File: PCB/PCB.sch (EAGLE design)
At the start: 43 parts, among them Q1 11.0592MHz

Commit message: Added adithya's files after verification
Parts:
- added PLED: (no value), led:LED5MM
- C4: value 10nF -> 0.1uF
- R1, R10, R11, R6, R7, R8: value (none) -> 10k
- R12, R17, R5: value (none) -> 1k
- R13, R14, R15, R2, R3, R4: value (none) -> 4.7k
- R9: value (none) -> 2.7k
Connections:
- removed net 555_O/P: 555_TIMER.3, R12.2
- new net N$15: PLED.A, R17.1
- net +10V: now also R14.1; no longer R15.1, R8.1
- net +5V: now also R17.2; no longer CD4029_1.10, CD4029_1.9, CD4029_2.10, CD4029_2.9
- net -10V: now also R8.1
- net A2: now also CD4029_2.14; no longer CD4029_2.11
- net A3: now also CD4029_2.11; no longer CD4029_2.14
- net CLK: now also 555_TIMER.3; no longer R12.1, R13.2
- net GND: now also CD4029_1.10, CD4029_1.9, CD4029_2.10, CD4029_2.9, PLED.C, R12.2, R16.1; no longer R14.1, R17.1
- net IOUT2: now also R15.2; no longer R16.2
- net N$11: now also R13.2; no longer R14.2
- net N$12: now also R14.2; no longer R15.2
- net N$33: now also R16.2; no longer R17.2
- net OUTPUT: now also R12.1, R15.1; no longer R16.1
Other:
- moved on the sheet: R12, R13, R14, R15, R16, R17, TP2

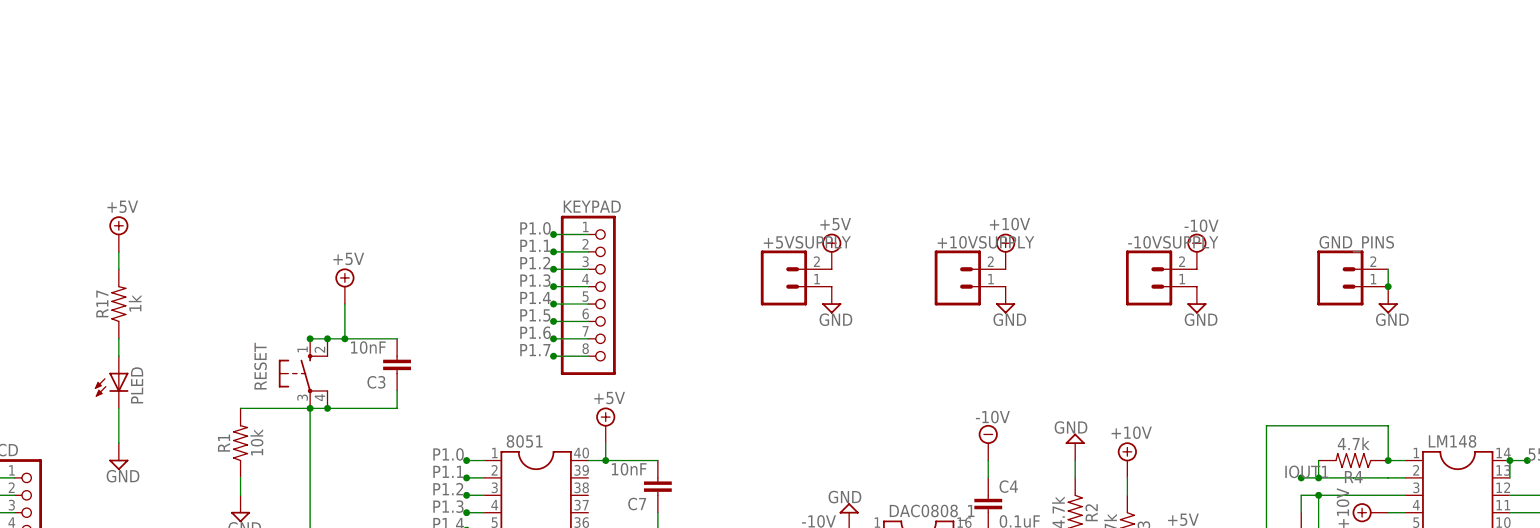
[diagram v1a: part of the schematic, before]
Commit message: Silkscreen, mounting holes, power/ip screw terminals
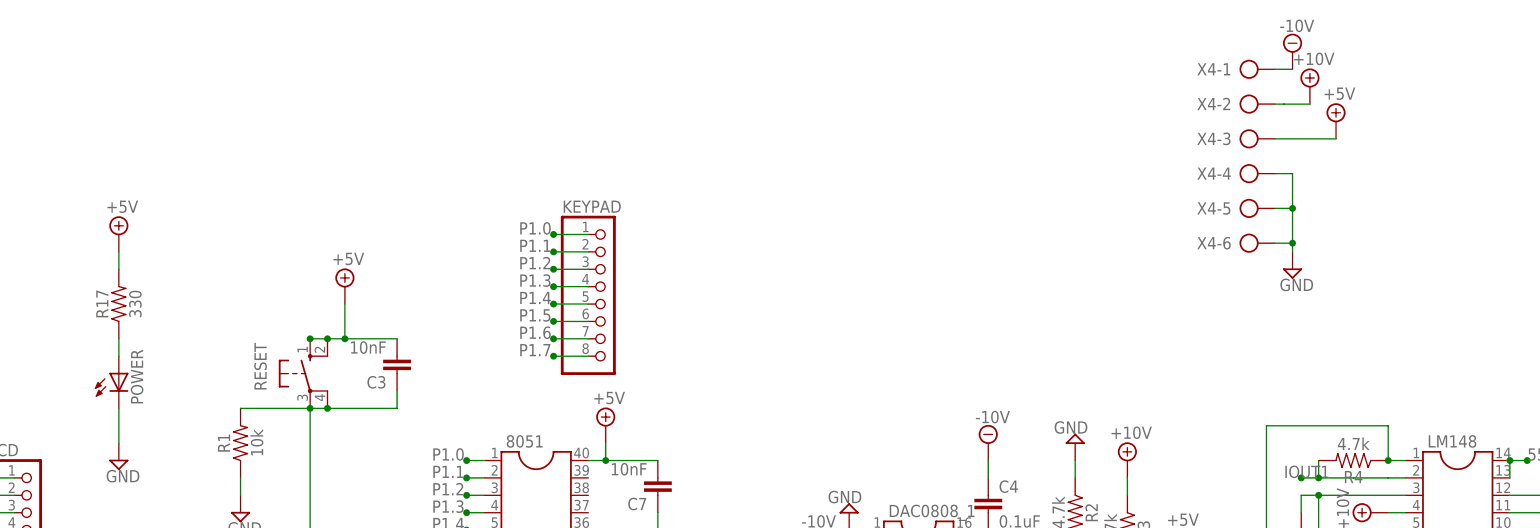
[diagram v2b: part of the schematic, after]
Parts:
- removed +10VSUPPLY, +5VSUPPLY, -10VSUPPLY, GND_PINS: (no value), SparkFun-Connectors:CONN_02
- added X4: (no value), con-ptr500:AK500/6-H
- R17: value 1k -> 330
- renumbered PLED to POWER
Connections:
- net +10V: now also X4-2.KL; no longer +10VSUPPLY.2
- net +5V: now also X4-3.KL; no longer +5VSUPPLY.2
- net -10V: now also X4-1.KL; no longer -10VSUPPLY.2
- net GND: now also X4-4.KL, X4-5.KL, X4-6.KL; no longer +10VSUPPLY.1, +5VSUPPLY.1, -10VSUPPLY.1, GND_PINS.1, GND_PINS.2

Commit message: Final-for manufacturing
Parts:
- added C8: 10nF, rcl:C-EU025-025X050
- added JP1, JP2, SJ1, SJ2, SJ3, SJ4, SJ5, SJ6, SJ7, SJ8: (no value), jumper:SJ
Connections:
- new net CD1-CLK: CD4029_1.15, SJ8.1
- new net CD2-CLK: CD4029_2.15, SJ5.1
- new net N$16: DAC0808_1.14, SJ2.1
- new net OP-555-CTRL: LM148.13, LM148.14, SJ6.1
- new net OPAMP-O/P: IC741.6, JP1.2, R12.1, R15.1, SJ3.1
- net +5V: now also JP2.2
- net 555_CONTROL: now also SJ6.2, SJ7.2; no longer LM148.13, LM148.14
- net CLK: now also SJ5.2, SJ8.2; no longer CD4029_1.15, CD4029_2.15
- net GND: now also C8.1, JP1.1, SJ1.1, SJ4.1, SJ7.1
- net N$2: now also SJ2.2; no longer DAC0808_1.14
- net N$4: now also SJ4.2
- net N$5: now also SJ1.2
- net OUTPUT: now also C8.2, SJ3.2; no longer IC741.6, R12.1, R15.1
- net RESET: now also JP2.1
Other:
- moved on the sheet: TP1

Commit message: Commit since not sure if any changes are made
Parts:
- 555_TIMER, C1, C2, C3, C4, C5, C6, C7, CD4029_1, CD4029_2, D1, DAC0808_1, DAC0808_2, IC741, JP1, JP2, KEYPAD, LCD, LM148, POWER, R1, R10, R11, R12, R13, R14, R15, R16, R17, R2, R3, R4, R5, R6, R7, R8, R9, SJ1, SJ2, SJ3, SJ4, SJ5, SJ6, SJ7, SJ8, TP1, TP2, X4: OC_FARNELL (none) -> unknown
- 8051: MF (none) -> OLIMEX; MPN (none) -> PIC-USB-4550; OC_FARNELL (none) -> 1701541
- C8: value 10nF -> .1u; OC_FARNELL (none) -> unknown
- Q1: MF (none) -> MULTICOMP; MPN (none) -> HC49SM-3.6864-30-50-60-16-ATF
- RESET: MF (none) -> OMRON

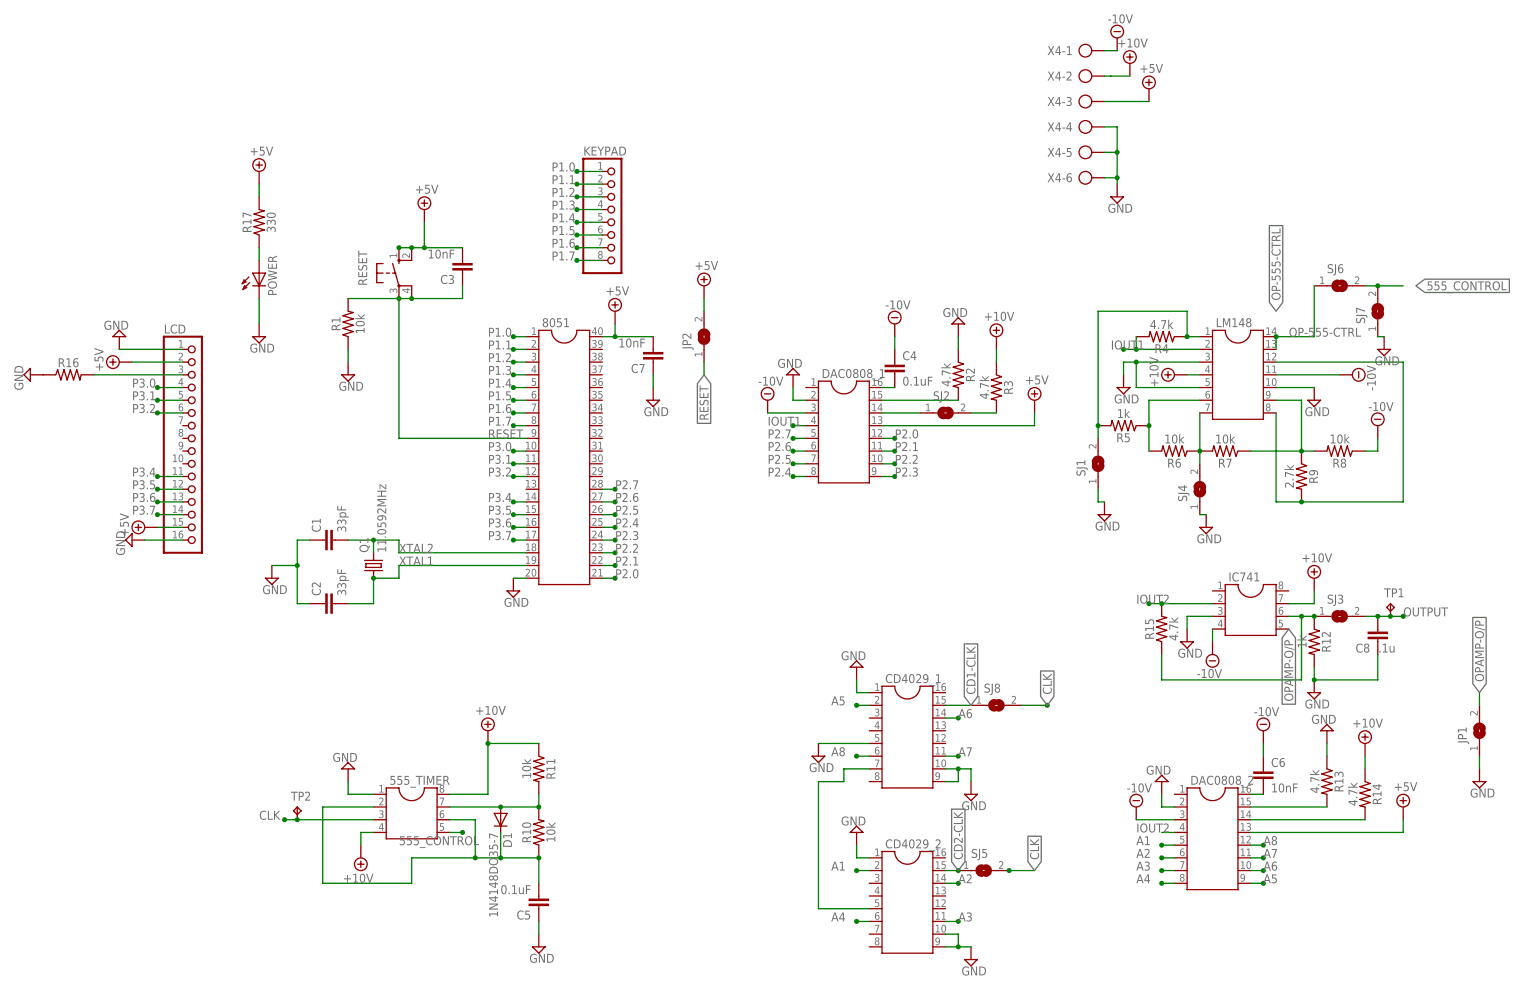
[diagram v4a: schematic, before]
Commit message: During assembly - changed some values
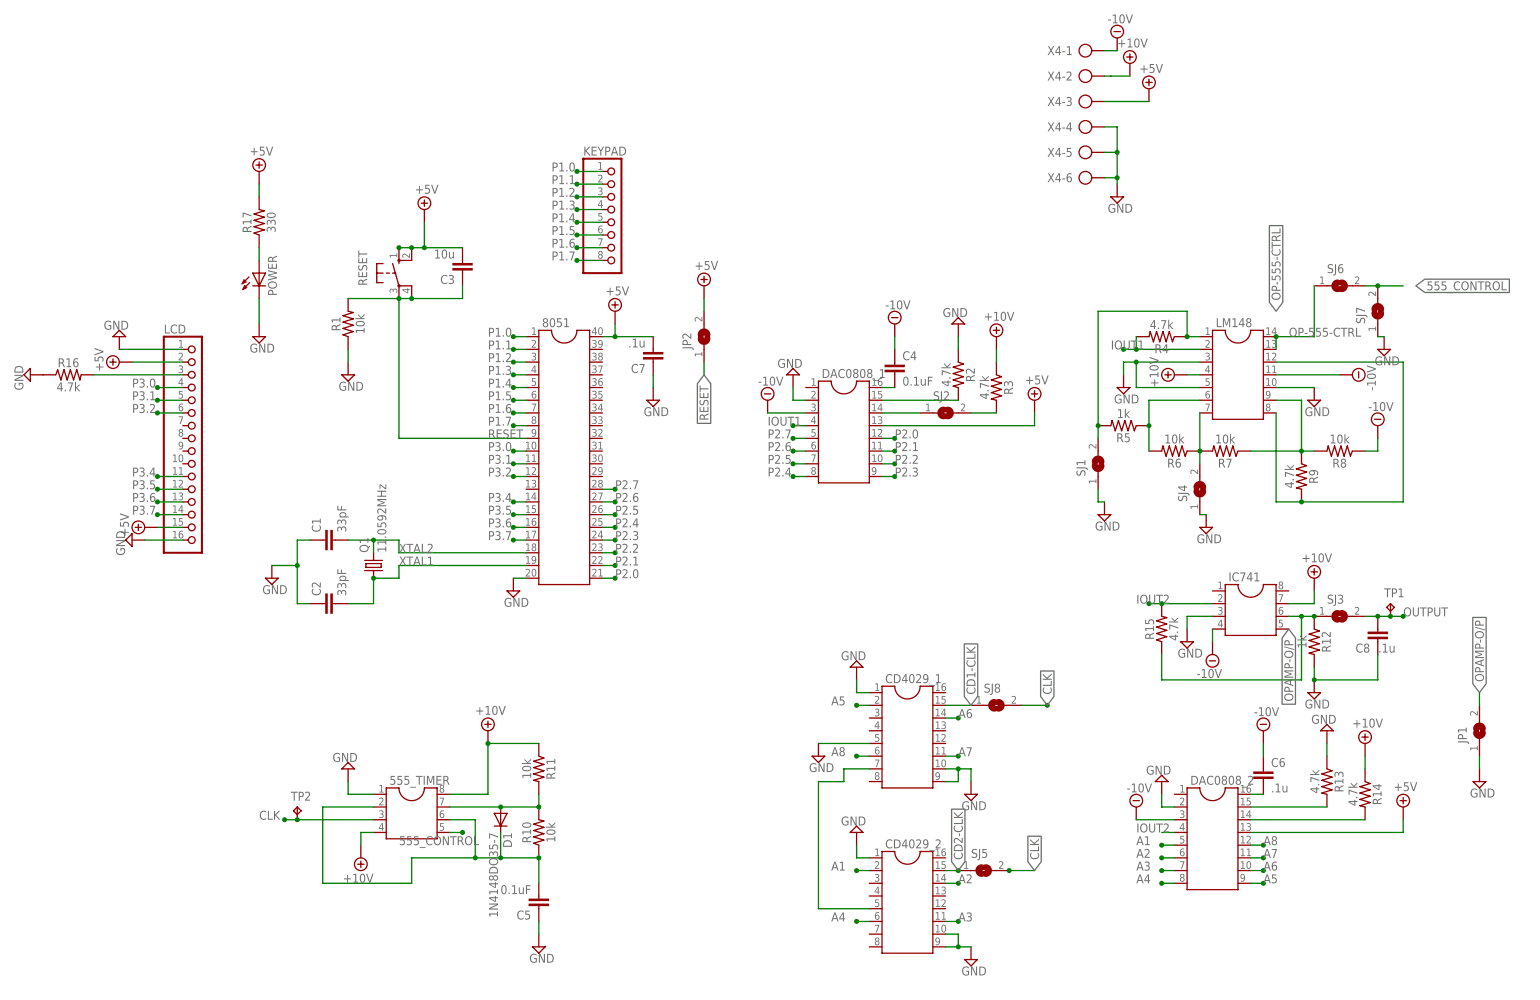
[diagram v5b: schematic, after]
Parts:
- C3: value 10nF -> 10u
- C6, C7: value 10nF -> .1u
- R16: value (none) -> 4.7k
- R9: value 2.7k -> 4.7k
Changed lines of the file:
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@@
 <attribute name="OC_FARNELL" value="unknown"/>
 </part>
-<part name="C3" library="rcl" library_urn="urn:adsk.eagle:library:334" deviceset="C-EU" device="025-025X050" package3d_urn="urn:adsk.eagle:package:23629/2" value="10nF">
+<part name="C3" library="rcl" library_urn="urn:adsk.eagle:library:334" deviceset="C-EU" device="025-025X050" package3d_urn="urn:adsk.eagle:package:23629/2" value="10u">
 <spice>
 <pinmapping spiceprefix="C">
@@
 <attribute name="OC_FARNELL" value="unknown"/>
 </part>
-<part name="R9" library="SparkFun-Resistors" library_urn="urn:adsk.eagle:library:532" deviceset="RESISTOR" device="AXIAL-0.3" package3d_urn="urn:adsk.eagle:package:39658/1" value="2.7k">
+<part name="R9" library="SparkFun-Resistors" library_urn="urn:adsk.eagle:library:532" deviceset="RESISTOR" device="AXIAL-0.3" package3d_urn="urn:adsk.eagle:package:39658/1" value="4.7k">
 <attribute name="MF" value=""/>
 <attribute name="MPN" value=""/>
@@
 <part name="SUPPLY24" library="supply2" library_urn="urn:adsk.eagle:library:372" deviceset="GND" device=""/>
 <part name="SUPPLY25" library="supply2" library_urn="urn:adsk.eagle:library:372" deviceset="GND" device=""/>
-<part name="C6" library="rcl" library_urn="urn:adsk.eagle:library:334" deviceset="C-EU" device="025-025X050" package3d_urn="urn:adsk.eagle:package:23629/2" value="10nF">
+<part name="C6" library="rcl" library_urn="urn:adsk.eagle:library:334" deviceset="C-EU" device="025-025X050" package3d_urn="urn:adsk.eagle:package:23629/2" value=".1u">
 <spice>
 <pinmapping spiceprefix="C">
@@
 <attribute name="OC_FARNELL" value="unknown"/>
 </part>
-<part name="R16" library="SparkFun-Resistors" library_urn="urn:adsk.eagle:library:532" deviceset="RESISTOR" device="AXIAL-0.3" package3d_urn="urn:adsk.eagle:package:39658/1" value=" ">
+<part name="R16" library="SparkFun-Resistors" library_urn="urn:adsk.eagle:library:532" deviceset="RESISTOR" device="AXIAL-0.3" package3d_urn="urn:adsk.eagle:package:39658/1" value="4.7k">
 <attribute name="MF" value=""/>
 <attribute name="MPN" value=""/>
@@
 <attribute name="OC_FARNELL" value="unknown"/>
 </part>
-<part name="C7" library="rcl" library_urn="urn:adsk.eagle:library:334" deviceset="C-EU" device="025-025X050" package3d_urn="urn:adsk.eagle:package:23629/2" value="10nF">
-<spice>
-<pinmapping spiceprefix="C">
+<part name="C7" library="rcl" library_urn="urn:adsk.eagle:library:334" deviceset="C-EU" device="025-025X050" package3d_urn="urn:adsk.eagle:package:23629/2" value=".1u">
+<spice>
+<pinmapping spiceprefix="C">
